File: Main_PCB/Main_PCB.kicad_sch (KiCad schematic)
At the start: 1 part, among them U1 ESP32-DEVKITC

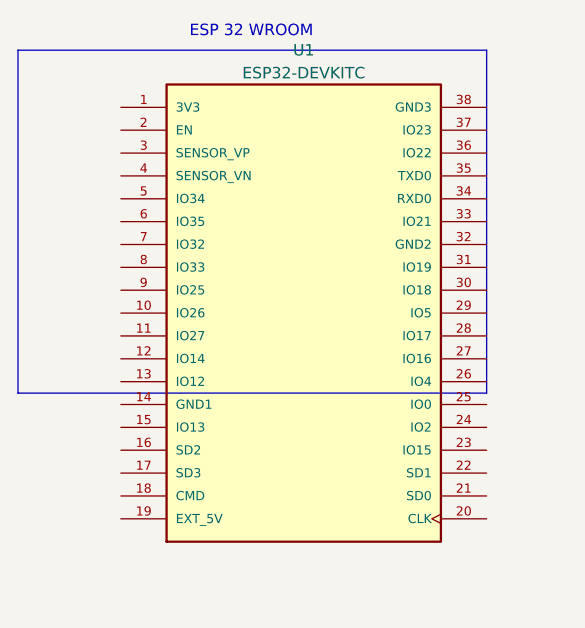
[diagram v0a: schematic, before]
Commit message: Changed footprint over
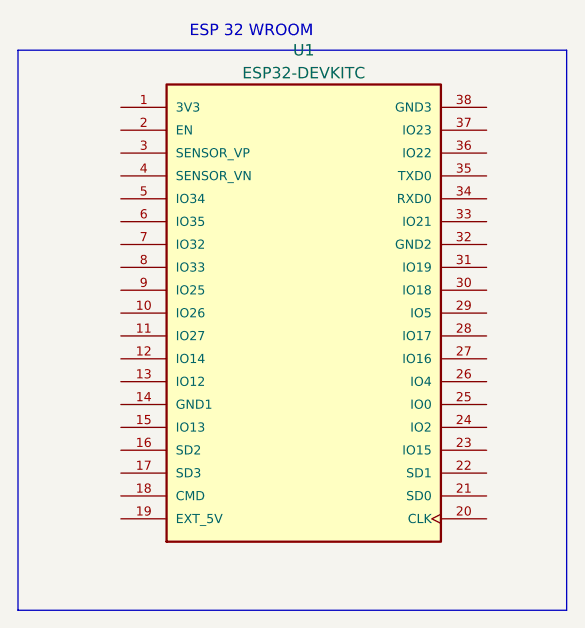
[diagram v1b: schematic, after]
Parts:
- U1: footprint MODULE_ESP32-DEVKITC -> Espressif:ESP32-WROOM-32E
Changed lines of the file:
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@@
 (kicad_sch (version 20230121) (generator eeschema)
   (paper "A4")
-  (rectangle (start 19.05 20.32) (end 71.12 58.42)
+  (rectangle (start 19.05 20.32) (end 80.01 82.55)
     (stroke (width 0) (type default))
     (fill (type none))
@@
       (effects (font (size 1.27 1.27)))
     )
-    (property "Footprint" "MODULE_ESP32-DEVKITC" (at 50.8 49.53 0)
+    (property "Footprint" "Espressif:ESP32-WROOM-32E" (at 50.8 49.53 0)
       (effects (font (size 1.27 1.27)) (justify bottom) hide)
     )
